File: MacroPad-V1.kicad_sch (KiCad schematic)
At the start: 0 parts

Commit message: update 1
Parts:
- added R1: 10k, symbol Device:R
- added SW1, SW10, SW11, SW12, SW2, SW3, SW4, SW5, SW6, SW7, SW8, SW9: SW_DIP_x01, symbol Switch:SW_DIP_x01
- added SW13, SW14, SW15: PEC11L-4220F-S0015, PEC11L-4xxxF-Sxxxx_BRN, symbol PEC11L_4220F_S0015:PEC11L-4220F-S0015
- added U1: PCA9555APW_118, PCA9555APW_118:SOP65P640X110-24N, symbol PCA9555APW_118:PCA9555APW_118
- added U2: Seeed Studio XIAO SAMD21, symbol Seeed_Studio_XIAO_Series:Seeed Studio XIAO SAMD21
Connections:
- new net: R1.2, U1.1 (~{INT})
- new net +3.3V: R1.1, SW1.1, SW10.1, SW11.1, SW12.1, SW2.1, SW3.1, SW4.1, SW5.1, SW6.1, SW7.1, SW8.1, SW9.1, U1.24 (VDD), U2.12 (3V3)
- new net +5V: U2.14 (5V), U2.15 (5V)
- new net A0: U2.1 (PA02_A0_D0)
- new net A1: U2.2 (PA4_A1_D1)
- new net A2: U2.3 (PA10_A2_D2)
- new net D3: U1.21 (A0), U2.4 (PA11_A3_D3)
- new net D6: U1.2 (A1), U2.7 (PB08_A6_D6_TX)
- new net D7: U1.3 (A2), U2.8 (PB09_A7_D7_RX)
- new net GND: U1.12 (VSS), U2.13 (GND), U2.16 (GND), U2.20 (GND)
- new net SCL: U1.22 (SCL), U2.6 (PA9_A5_D5_SCL)
- new net SDA: U1.23 (SDA), U2.5 (PA8_A4_D4_SDA)

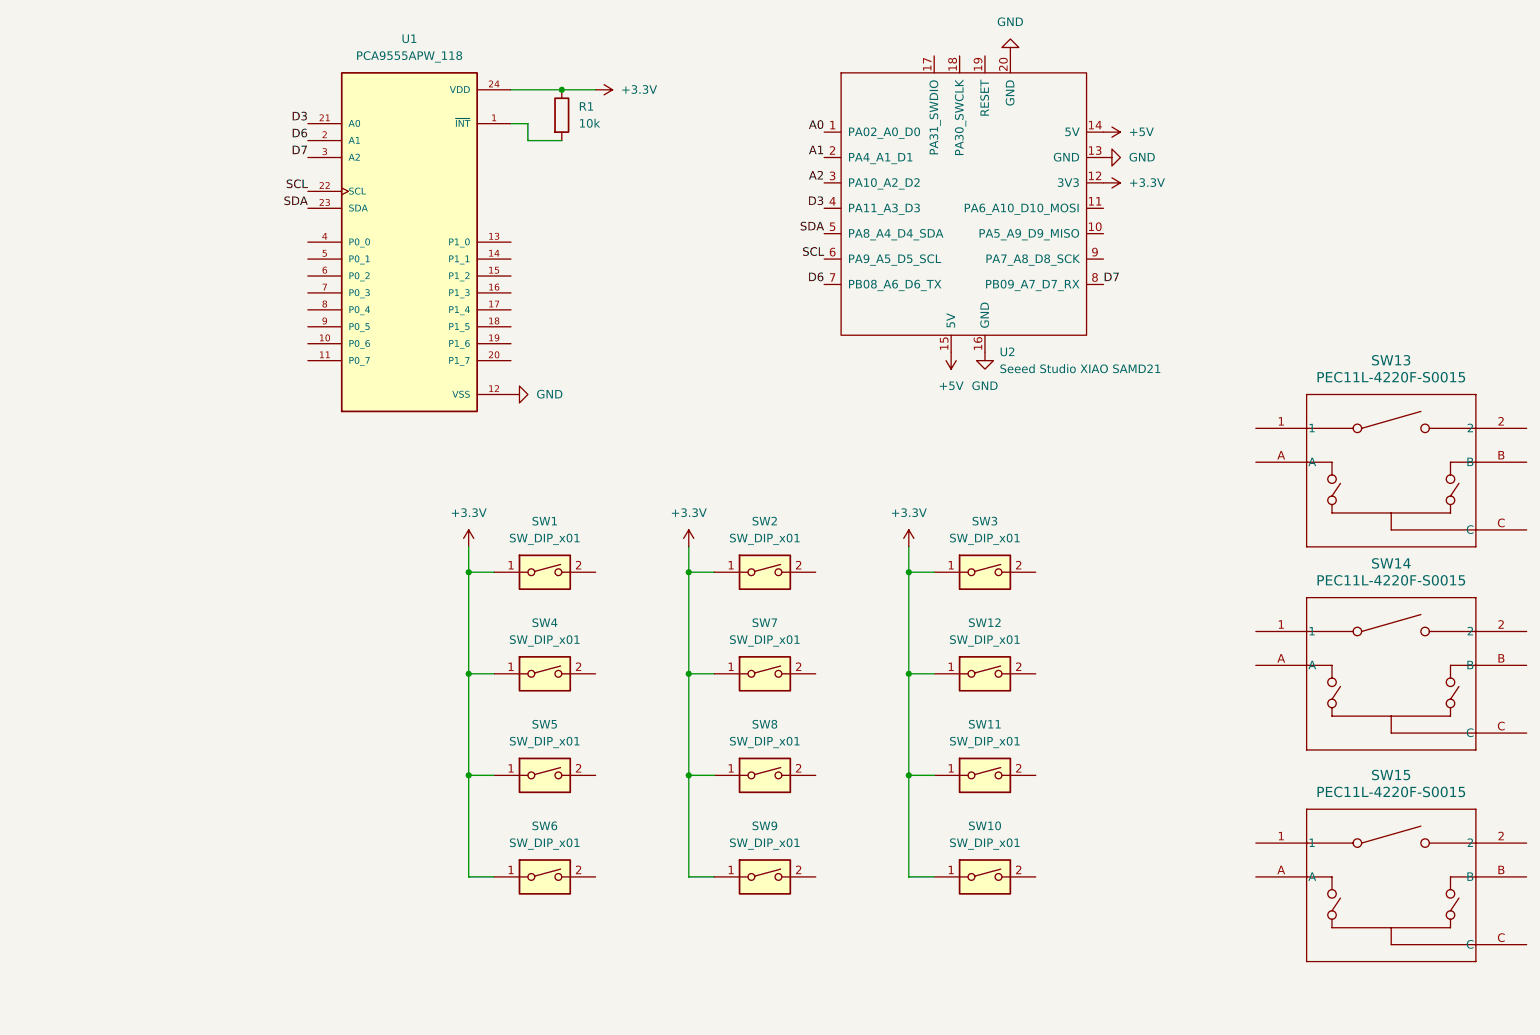
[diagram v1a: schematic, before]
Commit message: added wires from gpio extender to switches
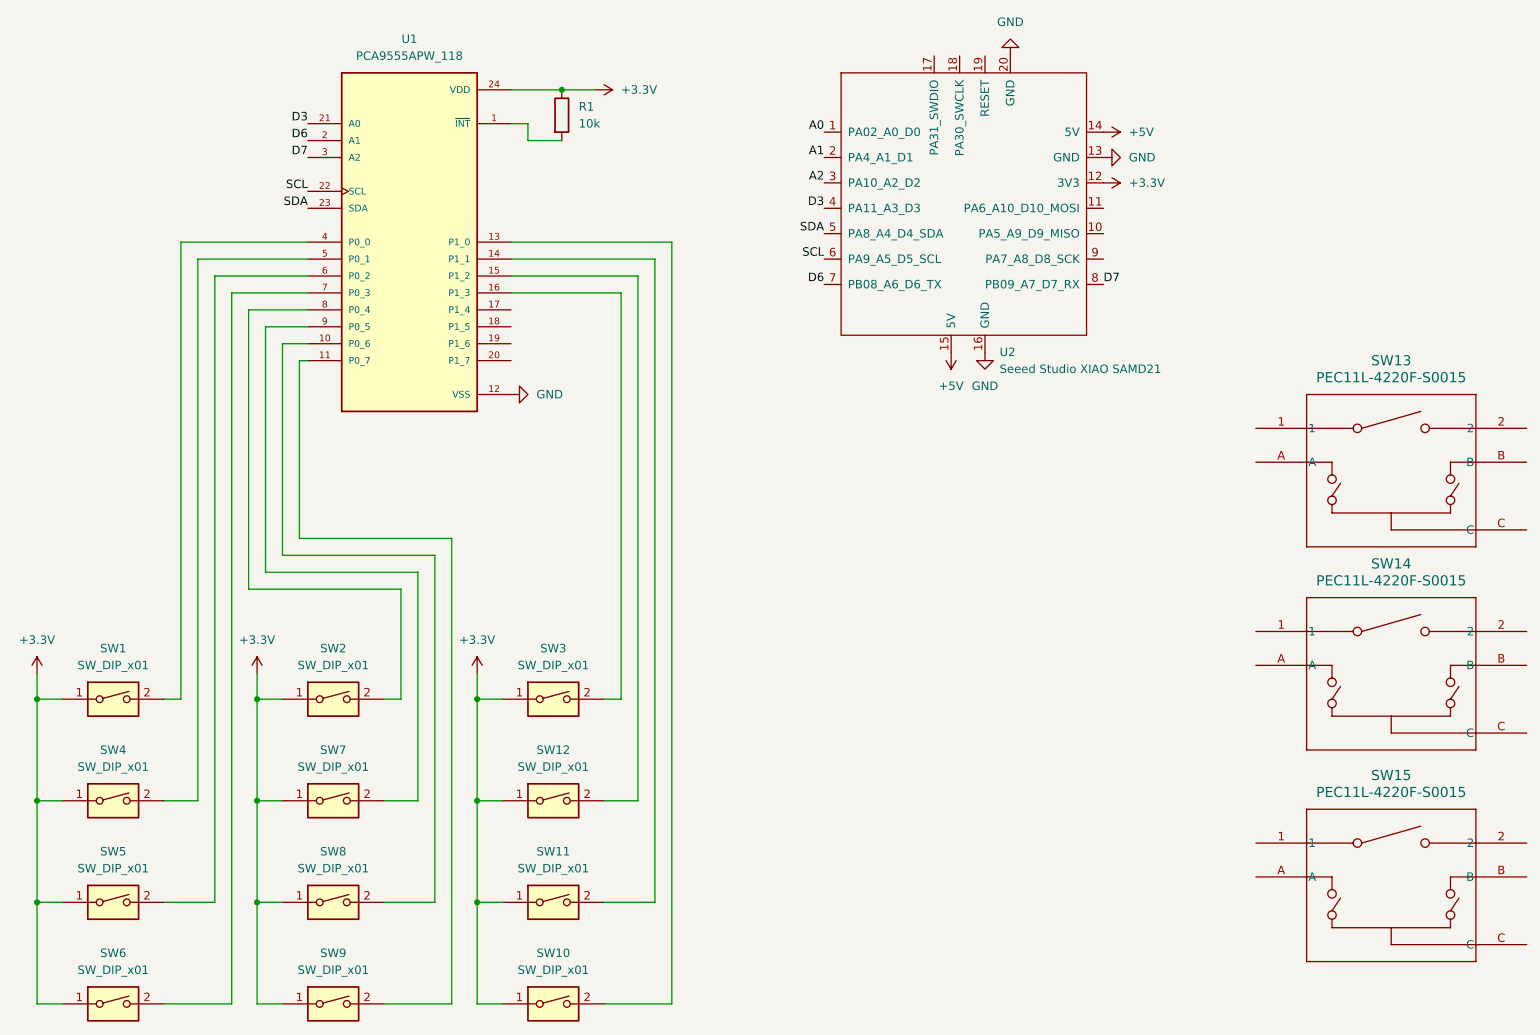
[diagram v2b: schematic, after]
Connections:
- net at SW10.2: now also U1.13 (P1_0)
- net at SW2.2: now also U1.8 (P0_4)
- net at U1.10 (P0_6): now also SW8.2
- net at U1.11 (P0_7): now also SW9.2
- net at U1.14 (P1_1): now also SW11.2
- net at U1.15 (P1_2): now also SW12.2
- net at U1.16 (P1_3): now also SW3.2
- net at U1.4 (P0_0): now also SW1.2
- net at U1.5 (P0_1): now also SW4.2
- net at U1.6 (P0_2): now also SW5.2
- net at U1.7 (P0_3): now also SW6.2
- net at U1.9 (P0_5): now also SW7.2
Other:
- moved on the sheet: SW1, SW10, SW11, SW12, SW2, SW3, SW4, SW5, SW6, SW7, SW8, SW9
